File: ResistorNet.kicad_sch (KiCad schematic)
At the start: 2 parts, among them J23 61300211121

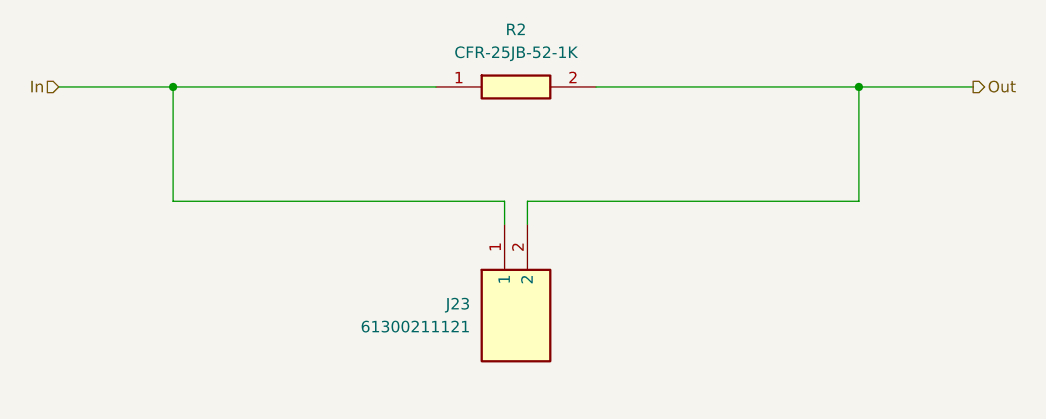
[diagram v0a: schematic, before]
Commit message: Updated re-annotated the schematics, created new PCB based on standards and updated components.
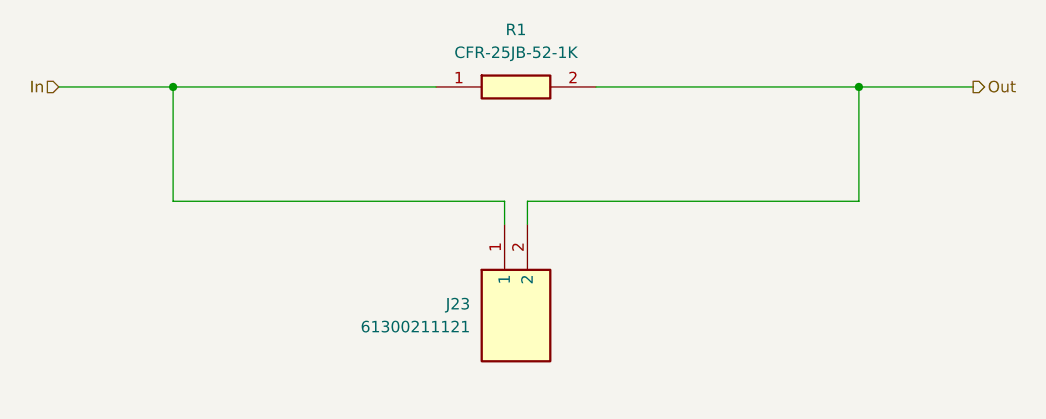
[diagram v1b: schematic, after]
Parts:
- R1: renamed from R2; footprint SamacSys_Parts:RESAD1590W60L630D240 -> Resistor_THT:R_Axial_DIN0204_L3.6mm_D1.6mm_P7.62mm_Horizontal
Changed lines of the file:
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@@
 		(dnp no)
 		(fields_autoplaced yes)
-		(property "Reference" "R2"
+		(property "Reference" "R1"
 			(at 139.7 82.55 0)
 			(effects
@@
 			)
 		)
-		(property "Footprint" "SamacSys_Parts:RESAD1590W60L630D240"
+		(property "Footprint" "Resistor_THT:R_Axial_DIN0204_L3.6mm_D1.6mm_P7.62mm_Horizontal"
 			(at 144.78 185.09 0)
 			(effects
@@
 			(project ""
 				(path "/1ab818d2-1673-4bd5-b77a-2cfddf9e3efa/0087dda1-1fbb-4bc9-8ac0-467f27dda043"
+					(reference "R3")
+					(unit 1)
+				)
+				(path "/1ab818d2-1673-4bd5-b77a-2cfddf9e3efa/062feb6c-41bf-40d6-b5fc-5815da19f51a"
+					(reference "R1")
+					(unit 1)
+				)
+				(path "/1ab818d2-1673-4bd5-b77a-2cfddf9e3efa/1c2d175d-5260-45e2-ab58-11f478a57245"
+					(reference "R12")
+					(unit 1)
+				)
+				(path "/1ab818d2-1673-4bd5-b77a-2cfddf9e3efa/34ccdcef-c5cd-45f8-8fd7-298a4c625fee"
+					(reference "R10")
+					(unit 1)
+				)
+				(path "/1ab818d2-1673-4bd5-b77a-2cfddf9e3efa/4c670f04-2e05-4e02-8866-f48372fa1ff8"
+					(reference "R2")
+					(unit 1)
+				)
+				(path "/1ab818d2-1673-4bd5-b77a-2cfddf9e3efa/599810dd-7f87-40b0-a78f-cf1fd654ab05"
+					(reference "R6")
+					(unit 1)
+				)
+				(path "/1ab818d2-1673-4bd5-b77a-2cfddf9e3efa/5ce1397b-840b-4c86-b2b8-476529fad0df"
+					(reference "R15")
+					(unit 1)
+				)
+				(path "/1ab818d2-1673-4bd5-b77a-2cfddf9e3efa/6be4737e-6b71-4d0f-95a0-61b7e1b4b4ed"
 					(reference "R4")
 					(unit 1)
 				)
-				(path "/1ab818d2-1673-4bd5-b77a-2cfddf9e3efa/062feb6c-41bf-40d6-b5fc-5815da19f51a"
-					(reference "R2")
+				(path "/1ab818d2-1673-4bd5-b77a-2cfddf9e3efa/6da8951b-55dd-49d3-848d-df84e1cdcf32"
+					(reference "R9")
 					(unit 1)
 				)
-				(path "/1ab818d2-1673-4bd5-b77a-2cfddf9e3efa/1c2d175d-5260-45e2-ab58-11f478a57245"
+				(path "/1ab818d2-1673-4bd5-b77a-2cfddf9e3efa/7efc8dc2-996f-46e9-97e2-641090acc2b3"
+					(reference "R16")
+					(unit 1)
+				)
+				(path "/1ab818d2-1673-4bd5-b77a-2cfddf9e3efa/858fe198-fd18-422f-af07-1edb2224c2e7"
+					(reference "R8")
+					(unit 1)
+				)
+				(path "/1ab818d2-1673-4bd5-b77a-2cfddf9e3efa/a2b5108e-5cbe-4e97-a861-4890393bd55d"
+					(reference "R5")
+					(unit 1)
+				)
+				(path "/1ab818d2-1673-4bd5-b77a-2cfddf9e3efa/a7dbdd01-c4ac-4031-af27-5a3f3ddfd29b"
+					(reference "R14")
+					(unit 1)
+				)
+				(path "/1ab818d2-1673-4bd5-b77a-2cfddf9e3efa/da21030a-0241-49ea-ba51-87bb18db145d"
 					(reference "R13")
 					(unit 1)
 				)
-				(path "/1ab818d2-1673-4bd5-b77a-2cfddf9e3efa/34ccdcef-c5cd-45f8-8fd7-298a4c625fee"
+				(path "/1ab818d2-1673-4bd5-b77a-2cfddf9e3efa/e2c9e78f-4350-49d8-b8bf-0d48f8fbb4ed"
+					(reference "R7")
+					(unit 1)
+				)
+				(path "/1ab818d2-1673-4bd5-b77a-2cfddf9e3efa/f6955642-3cf0-47c4-8e64-12dc958962ac"
 					(reference "R11")
 					(unit 1)
 				)
-				(path "/1ab818d2-1673-4bd5-b77a-2cfddf9e3efa/4c670f04-2e05-4e02-8866-f48372fa1ff8"
-					(reference "R3")
-					(unit 1)
-				)
-				(path "/1ab818d2-1673-4bd5-b77a-2cfddf9e3efa/599810dd-7f87-40b0-a78f-cf1fd654ab05"
-					(reference "R7")
-					(unit 1)
-				)
-				(path "/1ab818d2-1673-4bd5-b77a-2cfddf9e3efa/5ce1397b-840b-4c86-b2b8-476529fad0df"
-					(reference "R16")
-					(unit 1)
-				)
-				(path "/1ab818d2-1673-4bd5-b77a-2cfddf9e3efa/6be4737e-6b71-4d0f-95a0-61b7e1b4b4ed"
-					(reference "R5")
-					(unit 1)
-				)
-				(path "/1ab818d2-1673-4bd5-b77a-2cfddf9e3efa/6da8951b-55dd-49d3-848d-df84e1cdcf32"
-					(reference "R10")
-					(unit 1)
-				)
-				(path "/1ab818d2-1673-4bd5-b77a-2cfddf9e3efa/7efc8dc2-996f-46e9-97e2-641090acc2b3"
-					(reference "R17")
-					(unit 1)
-				)
-				(path "/1ab818d2-1673-4bd5-b77a-2cfddf9e3efa/858fe198-fd18-422f-af07-1edb2224c2e7"
-					(reference "R9")
-					(unit 1)
-				)
-				(path "/1ab818d2-1673-4bd5-b77a-2cfddf9e3efa/a2b5108e-5cbe-4e97-a861-4890393bd55d"
-					(reference "R6")
-					(unit 1)
-				)
-				(path "/1ab818d2-1673-4bd5-b77a-2cfddf9e3efa/a7dbdd01-c4ac-4031-af27-5a3f3ddfd29b"
-					(reference "R15")
-					(unit 1)
-				)
-				(path "/1ab818d2-1673-4bd5-b77a-2cfddf9e3efa/da21030a-0241-49ea-ba51-87bb18db145d"
-					(reference "R14")
-					(unit 1)
-				)
-				(path "/1ab818d2-1673-4bd5-b77a-2cfddf9e3efa/e2c9e78f-4350-49d8-b8bf-0d48f8fbb4ed"
-					(reference "R8")
-					(unit 1)
-				)
-				(path "/1ab818d2-1673-4bd5-b77a-2cfddf9e3efa/f6955642-3cf0-47c4-8e64-12dc958962ac"
-					(reference "R12")
-					(unit 1)
-				)

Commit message: Updated components to the custom library and applied additional standards.
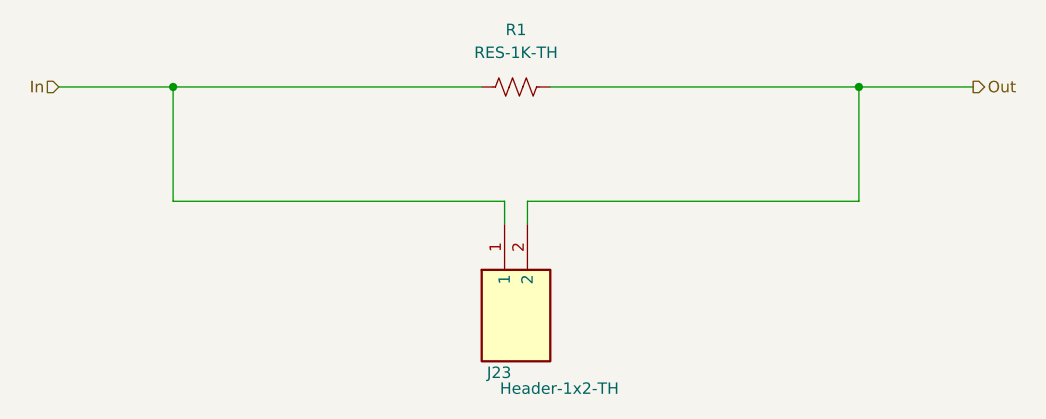
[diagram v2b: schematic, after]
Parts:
- J23: value 61300211121 -> Header-1x2-TH; footprint SamacSys_Parts:HDRV2W110P0X254_1X2_508X254X854P -> Custom:710-61300211121; symbol SamacSys_Parts:61300211121 -> Custom:Header-1x2-TH; Supplier (none) -> Mouser; Supplier Part Number (none) -> 710-61300211121; Supplier Price/Stock (none) -> https://www.mouser.co.uk/ProductDetail/Wurth-Elektronik/613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
- R1: value CFR-25JB-52-1K -> RES-1K-TH; symbol SamacSys_Parts:CFR-25JB-52-1K -> Custom:Res-1K-TH; Manufacturer_Name KEMET -> YAGEO; Manufacturer_Part_Number CFR-25JB-52-1K -> CFR-25JR-52-1K; Supplier (none) -> Mouser; Supplier Part Number (none) -> 603-CFR-25JR-521K; Supplier Price/Stock (none) -> https://www.mouser.com/ProductDetail/YAGEO/CFR-25JR-52-1K?q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
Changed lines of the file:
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@@
 	(wire
 		(pts
-			(xy 101.6 88.9) (xy 130.81 88.9)
-		)
-		(stroke
-			(width 0)
-			(type default)
-		)
-	)
-	(wire
-		(pts
-			(xy 148.59 88.9) (xy 177.8 88.9)
+			(xy 101.6 88.9) (xy 135.89 88.9)
+		)
+		(stroke
+			(width 0)
+			(type default)
+		)
+	)
+	(wire
+		(pts
+			(xy 143.51 88.9) (xy 177.8 88.9)
 		)
 		(stroke
@@
 	)
 	(symbol
-		(lib_id "SamacSys_Parts:CFR-25JB-52-1K")
-		(at 130.81 88.9 0)
+		(lib_id "Custom:Res-1K-TH")
+		(at 139.7 88.9 90)
 		(unit 1)
 		(exclude_from_sim no)
@@
 		(fields_autoplaced yes)
 		(property "Reference" "R1"
-			(at 139.7 82.55 0)
-			(effects
-				(font
-					(size 1.27 1.27)
-				)
-			)
-		)
-		(property "Value" "CFR-25JB-52-1K"
-			(at 139.7 85.09 0)
+			(at 139.7 82.55 90)
+			(effects
+				(font
+					(size 1.27 1.27)
+				)
+			)
+		)
+		(property "Value" "RES-1K-TH"
+			(at 139.7 85.09 90)
 			(effects
 				(font
@@
 		)
 		(property "Footprint" "Resistor_THT:R_Axial_DIN0204_L3.6mm_D1.6mm_P7.62mm_Horizontal"
-			(at 144.78 185.09 0)
-			(effects
-				(font
-					(size 1.27 1.27)
-				)
-				(justify left top)
-				(hide yes)
-			)
-		)
-		(property "Datasheet" ""
-			(at 144.78 285.09 0)
-			(effects
-				(font
-					(size 1.27 1.27)
-				)
-				(justify left top)
-				(hide yes)
-			)
-		)
-		(property "Description" "Carbon Film Resistors - Through Hole 1/4W 1K Ohm 5%"
-			(at 130.81 88.9 0)
+			(at 139.954 87.884 90)
+			(effects
+				(font
+					(size 1.27 1.27)
+				)
+				(hide yes)
+			)
+		)
+		(property "Datasheet" "https://www.mouser.com/datasheet/3/508/1/YAGEO%20CFR_datasheet_2023v2.pdf"
+			(at 139.7 88.9 0)
+			(effects
+				(font
+					(size 1.27 1.27)
+				)
+				(hide yes)
+			)
+		)
+		(property "Description" "Resistor - 1K- 1/4W - 5% - Through Hole"
+			(at 139.7 88.9 0)
 			(effects
 				(font
@@
 		)
 		(property "Height" ""
-			(at 144.78 485.09 0)
+			(at 535.89 74.93 0)
 			(effects
 				(font
@@
 		)
 		(property "Mouser Part Number" "N/A"
-			(at 144.78 585.09 0)
+			(at 635.89 74.93 0)
 			(effects
 				(font
@@
 		)
 		(property "Mouser Price/Stock" "https://www.mouser.co.uk/ProductDetail/Yageo/CFR-25JB-52-1K/?qs=oypCK0zG326Dzm6bUFS4DQ%3D%3D"
-			(at 144.78 685.09 0)
-			(effects
-				(font
-					(size 1.27 1.27)
-				)
-				(justify left top)
-				(hide yes)
-			)
-		)
-		(property "Manufacturer_Name" "KEMET"
-			(at 144.78 785.09 0)
-			(effects
-				(font
-					(size 1.27 1.27)
-				)
-				(justify left top)
-				(hide yes)
-			)
-		)
-		(property "Manufacturer_Part_Number" "CFR-25JB-52-1K"
-			(at 144.78 885.09 0)
-			(effects
-				(font
-					(size 1.27 1.27)
-				)
-				(justify left top)
+			(at 735.89 74.93 0)
+			(effects
+				(font
+					(size 1.27 1.27)
+				)
+				(justify left top)
+				(hide yes)
+			)
+		)
+		(property "Manufacturer_Name" "YAGEO"
+			(at 139.7 88.9 0)
+			(effects
+				(font
+					(size 1.27 1.27)
+				)
+				(hide yes)
+			)
+		)
+		(property "Manufacturer_Part_Number" "CFR-25JR-52-1K "
+			(at 139.7 88.9 0)
+			(effects
+				(font
+					(size 1.27 1.27)
+				)
+				(hide yes)
+			)
+		)
+		(property "Supplier" "Mouser"
+			(at 139.7 88.9 0)
+			(effects
+				(font
+					(size 1.27 1.27)
+				)
+				(hide yes)
+			)
+		)
+		(property "Supplier Part Number" "603-CFR-25JR-521K"
+			(at 139.7 88.9 0)
+			(effects
+				(font
+					(size 1.27 1.27)
+				)
+				(hide yes)
+			)
+		)
+		(property "Supplier Price/Stock" "https://www.mouser.com/ProductDetail/YAGEO/CFR-25JR-52-1K?qs=FK4oyhsNhknmd5zXOZ4mTQ%3D%3D"
+			(at 139.7 88.9 0)
+			(effects
+				(font
+					(size 1.27 1.27)
+				)
 				(hide yes)
 			)
@@
 	)
 	(symbol
-		(lib_id "SamacSys_Parts:61300211121")
+		(lib_id "Custom:Header-1x2-TH")
 		(at 138.43 104.14 90)
 		(mirror x)
@@
 		(dnp no)
 		(property "Reference" "J23"
-			(at 134.62 113.0299 90)
+			(at 139.192 120.65 90)
 			(effects
 				(font
@@
 			)
 		)
-		(property "Value" "61300211121"
-			(at 134.62 115.5699 90)
-			(effects
-				(font
-					(size 1.27 1.27)
-				)
-				(justify left)
-			)
-		)
-		(property "Footprint" "SamacSys_Parts:HDRV2W110P0X254_1X2_508X254X854P"
+		(property "Value" "Header-1x2-TH"
+			(at 151.13 121.666 90)
+			(effects
+				(font
+					(size 1.27 1.27)
+				)
+				(justify left top)
+			)
+		)
+		(property "Footprint" "Custom:710-61300211121"
 			(at 233.35 120.65 0)
 			(effects
@@
 			)
 		)
-		(property "Description" "WR-PHD 2.54 mm Pin Header 2 pins, 1 row, straight, gold plating"
+		(property "Description" "Header - WR-PHD 2.54 mm Pin Header 2 pins, 1 row, straight, gold plating"
 			(at 138.43 104.14 0)
 			(effects
@@
 			(effects
 				(font
+					(size 1.27 1.27)
+				)
+				(justify left top)
+				(hide yes)
+			)
+		)
+		(property "Supplier" "Mouser"
+			(at 138.43 104.14 0)
+			(effects
+				(font
+					(size 1.27 1.27)
+				)
+				(hide yes)
+			)
+		)
+		(property "Supplier Part Number" "710-61300211121"
+			(at 633.35 120.65 0)
+			(effects
+				(font
+					(size 1.27 1.27)
+				)
+				(justify left top)
+				(hide yes)
+			)
+		)
+		(property "Supplier Price/Stock" "https://www.mouser.co.uk/ProductDetail/Wurth-Elektronik/61300211121?qs=t4813l51qx%252B1A5GYDQxPlw%3D%3D"
+			(at 733.35 120.65 0)
+			(effects
+				(font

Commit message: Updated sheets with title, version, and date.  Corrected issue with resistor placement and connection on PowerLED module.
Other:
- title: (none) -> Arduino Light Controller - Resistor Module
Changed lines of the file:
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@@
 	(generator_version "9.0")
 	(paper "A4")
+	(title_block
+		(title "Arduino Light Controller - Resistor Module")
+		(date "2026-01-30")
+		(rev "1.1")
+	)
 	(junction
 		(at 177.8 88.9)
